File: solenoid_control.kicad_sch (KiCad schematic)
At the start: 39 parts, among them Q1 2N7002, Q10 DMG3406L, Q11 DMP3068L, Q12 DMG3406L, Q13 2N7002, Q14 DMP3068L, Q15 DMG3406L, Q16 DMP3068L, Q17 DMG3406L, Q19 2N7002, Q2 2N7002, Q3 DMP3068L, Q4 DMG3406L, Q5 DMP3068L, Q6 DMG3406L, Q7 2N7002, Q8 2N7002, Q9 DMP3068L

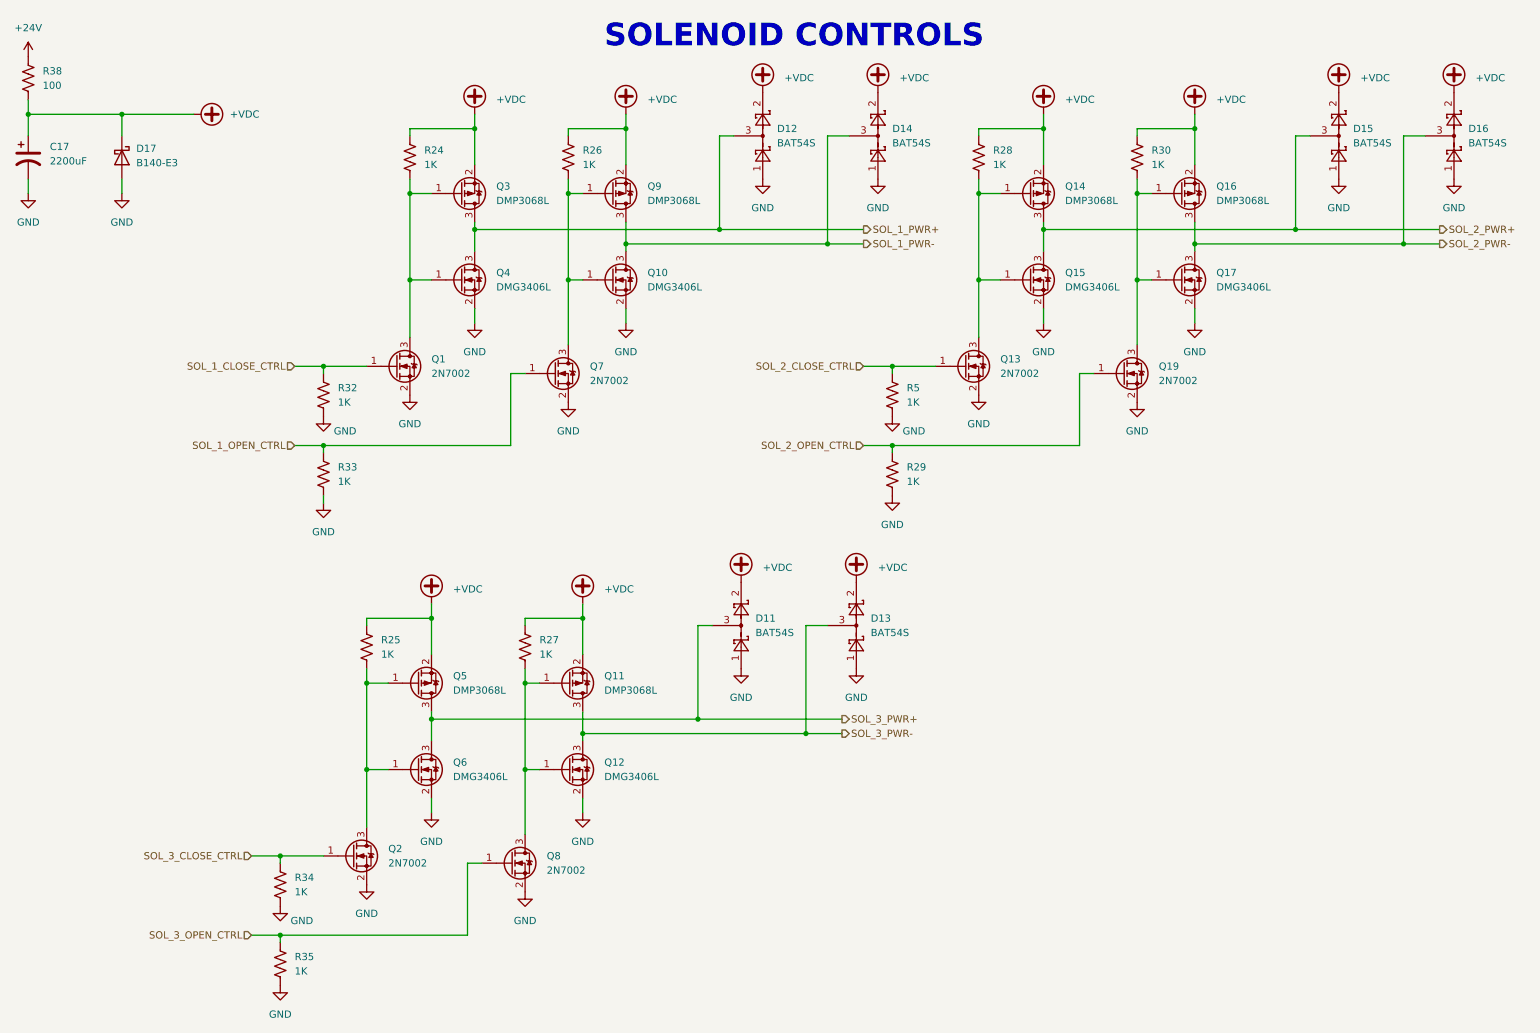
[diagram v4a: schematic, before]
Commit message: Replaced relays with smd versions.
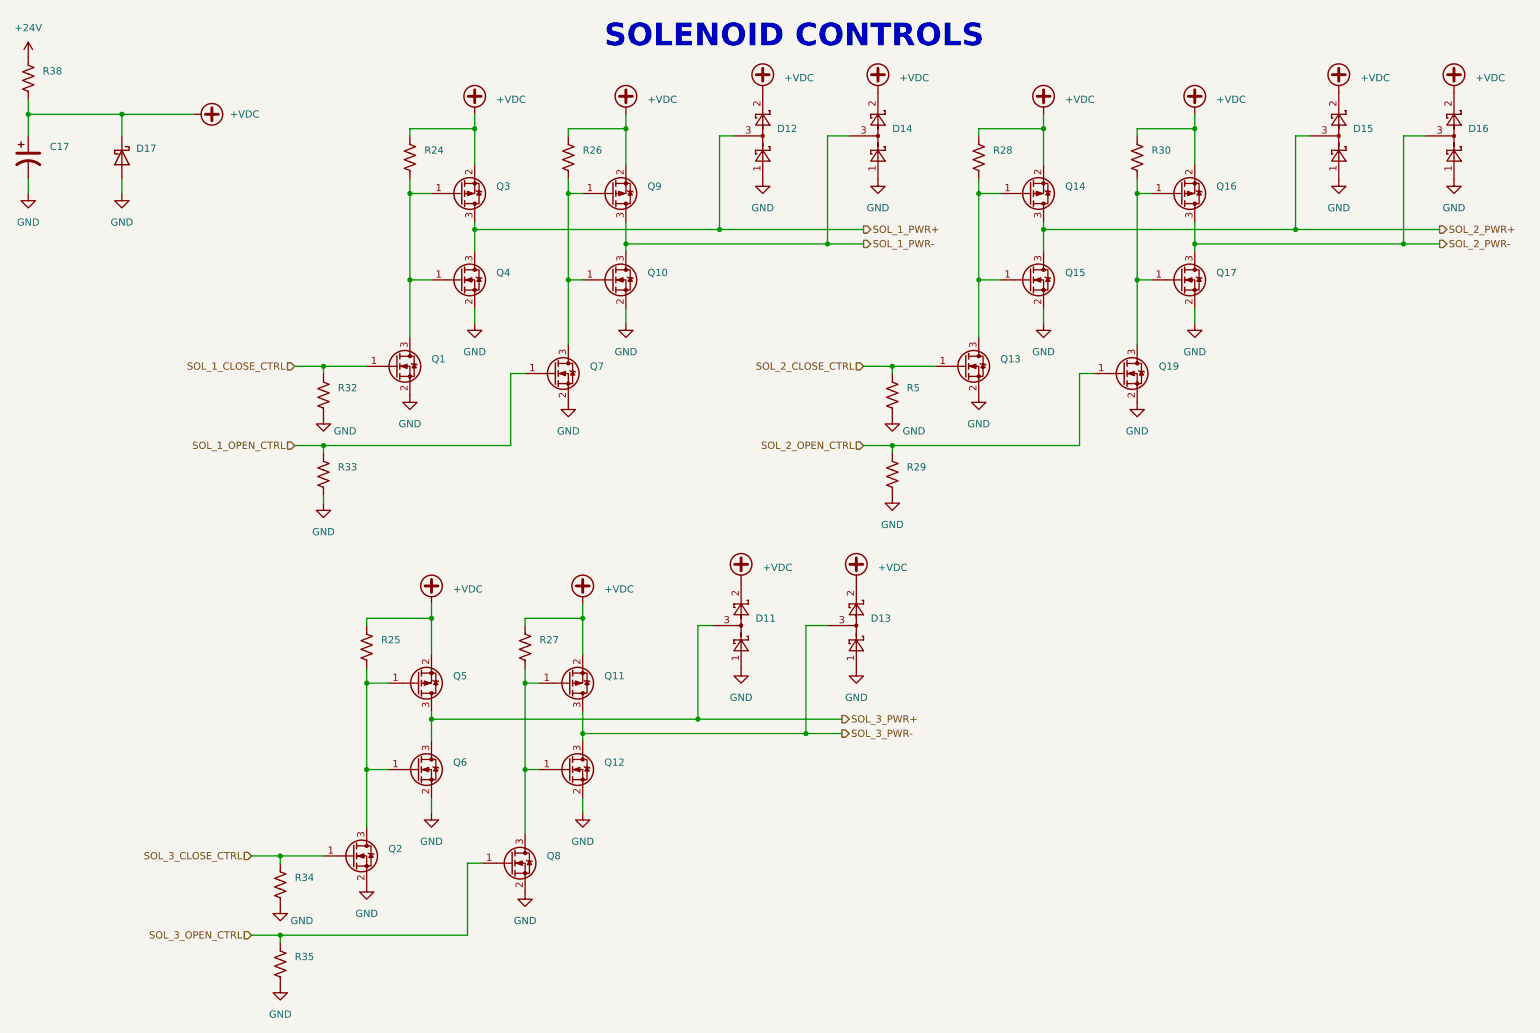
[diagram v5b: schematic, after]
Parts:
- C17: value 2200uF -> (none); footprint Capacitor_THT:CP_Radial_D16.0mm_P7.50mm -> (none)
- D11, D12, D13, D14, D15, D16: value BAT54S -> (none); footprint Package_TO_SOT_SMD:SOT-23 -> (none)
- D17: value B140-E3 -> (none); footprint Diode_SMD:D_SMA -> (none)
- Q1, Q13, Q19, Q2, Q7, Q8: value 2N7002 -> (none); footprint Package_TO_SOT_SMD:SOT-23 -> (none)
- Q10, Q12, Q15, Q17, Q4, Q6: value DMG3406L -> (none); footprint Package_TO_SOT_SMD:SOT-23 -> (none)
- Q11, Q14, Q16, Q3, Q5, Q9: value DMP3068L -> (none); footprint Package_TO_SOT_SMD:SOT-23 -> (none)
- R24, R25, R26, R27, R28, R29, R30, R32, R33, R34, R35, R5: value 1K -> (none); footprint Resistor_SMD:R_0805_2012Metric -> (none)
- R38: value 100 -> (none); footprint Resistor_SMD:R_2512_6332Metric -> (none)
